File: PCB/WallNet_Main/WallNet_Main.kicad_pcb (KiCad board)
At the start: 4 copper layers, 121.7 x 158.2 mm, 87 parts, among them J1 Conn_01x05_Pin, J101 USB_C_Receptacle_PowerOnly_6P, J102 01x04 Molex, J201 01x04 Molex, J202 Conn_01x07_Socket, J203 02x12 Connector, Q201 BSS138, SW1 SW, U1 BT832, U101 BQ25895RTWT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

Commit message: some random changes
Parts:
- moved R2 120.2 mm to (68.7, 106.0)
- moved D1 118.3 mm to (68.0, 100.5)
- moved C2 38.5 mm to (27.0, 23.5), turned to 90 degrees
- moved R1 33.3 mm to (21.5, 23.0), turned to -90 degrees
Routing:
- net VDD_nrf: track 12.1 -> 9.18 mm, vias 5 -> 4
- net GND: track 7.73 -> 5.27 mm, vias 3 -> 2
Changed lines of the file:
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@@
 	(footprint "Diode_SMD:D_0603_1608Metric"
 		(layer "F.Cu")
-		(at -16.2625 17.5 180)
+		(at 68 100.5 180)
 		(descr "Diode SMD 0603 (1608 Metric), square (rectangular) end terminal, IPC-7351 nominal, (Body size source: http://www.tortai-tech.com/upload/download/2011102023233369053.pdf), generated with kicad-footprint-generator")
 		(tags "diode")
@@
 	(footprint "Resistor_SMD:R_0603_1608Metric"
 		(layer "F.Cu")
-		(at -16.225 21 180)
+		(at 68.7125 106 180)
 		(descr "Resistor SMD 0603 (1608 Metric), square (rectangular) end terminal, IPC-7351 nominal, (Body size source: IPC-SM-782 page 72, https://www.pcb-3d.com/wordpress/wp-content/uploads/ipc-sm-782a_amendment_1_and_2.pdf), generated with kicad-footprint-generator")
 		(tags "resistor")
@@
 	(footprint "Capacitor_SMD:C_0603_1608Metric"
 		(layer "F.Cu")
-		(at -11.4 20.5 180)
+		(at 27 23.5 90)
 		(descr "Capacitor SMD 0603 (1608 Metric), square (rectangular) end terminal, IPC-7351 nominal, (Body size source: IPC-SM-782 page 76, https://www.pcb-3d.com/wordpress/wp-content/uploads/ipc-sm-782a_amendment_1_and_2.pdf), generated with kicad-footprint-generator")
 		(tags "capacitor")
 		(property "Reference" "C2"
-			(at 0 -1.43 0)
+			(at 0 -1.43 90)
 			(layer "F.SilkS")
 			(effects
@@
 		)
 		(property "Value" "100nF"
-			(at -2.85 -0.5 0)
+			(at -2.85 -0.5 90)
 			(layer "F.Fab")
 			(effects
@@
 		)
 		(property "Datasheet" "~"
-			(at 0 0 0)
+			(at 0 0 90)
 			(layer "F.Fab")
 			(hide yes)
@@
 		)
 		(property "Description" "Unpolarized capacitor, small symbol"
-			(at 0 0 0)
+			(at 0 0 90)
 			(layer "F.Fab")
 			(hide yes)
@@
 		(attr smd)
 		(fp_line
-			(start -0.14058 0.51)
-			(end 0.14058 0.51)
+			(start -0.14058 -0.51)
+			(end 0.14058 -0.51)
 			(stroke
 				(width 0.12)
@@
 		)
 		(fp_line
-			(start -0.14058 -0.51)
-			(end 0.14058 -0.51)
+			(start -0.14058 0.51)
+			(end 0.14058 0.51)
 			(stroke
 				(width 0.12)
@@
 		)
 		(fp_text user "${REFERENCE}"
-			(at 0 0 0)
+			(at 0 0 90)
 			(layer "F.Fab")
 			(effects
@@
 		)
 		(pad "1" smd roundrect
-			(at -0.775 0 180)
+			(at -0.775 0 90)
 			(size 0.9 0.95)
 			(layers "F.Cu" "F.Mask" "F.Paste")
@@
 		)
 		(pad "2" smd roundrect
-			(at 0.775 0 180)
+			(at 0.775 0 90)
 			(size 0.9 0.95)
 			(layers "F.Cu" "F.Mask" "F.Paste")
@@
 	(footprint "Resistor_SMD:R_0603_1608Metric"
 		(layer "F.Cu")
-		(at -11.4 17.99 180)
+		(at 21.5 23 -90)
 		(descr "Resistor SMD 0603 (1608 Metric), square (rectangular) end terminal, IPC-7351 nominal, (Body size source: IPC-SM-782 page 72, https://www.pcb-3d.com/wordpress/wp-content/uploads/ipc-sm-782a_amendment_1_and_2.pdf), generated with kicad-footprint-generator")
 		(tags "resistor")
 		(property "Reference" "R1"
-			(at -2.35 -0.01 0)
+			(at -2.35 -0.01 90)
 			(layer "F.SilkS")
 			(effects
@@
 		)
 		(property "Value" "10k"
-			(at 0 1.43 0)
+			(at 0 1.43 90)
 			(layer "F.Fab")
 			(effects
@@
 		)
 		(property "Datasheet" "~"
-			(at 0 0 0)
+			(at 0 0 90)
 			(layer "F.Fab")
 			(hide yes)
@@
 		)
 		(property "Description" "Resistor, small US symbol"
-			(at 0 0 0)
+			(at 0 0 90)
 			(layer "F.Fab")
 			(hide yes)
@@
 		)
 		(fp_text user "${REFERENCE}"
-			(at 0 0 0)
+			(at 0 0 90)
 			(layer "F.Fab")
 			(effects
@@
 		)
 		(pad "1" smd roundrect
-			(at -0.825 0 180)
+			(at -0.825 0 270)
 			(size 0.8 0.95)
 			(layers "F.Cu" "F.Mask" "F.Paste")
@@
 		)
 		(pad "2" smd roundrect
-			(at 0.825 0 180)
+			(at 0.825 0 270)
 			(size 0.8 0.95)
 			(layers "F.Cu" "F.Mask" "F.Paste")
@@
 		(fill no)
 		(layer "F.Cu")
-		(net 1)
+		(net 72)
 	)
 	(gr_rect
@@
 	)
 	(segment
-		(start -15.475 16.075)
-		(end -15.475 17.5)
-		(width 0.1524)
-		(layer "F.Cu")
-		(net 1)
-	)
-	(segment
 		(start 15 47)
 		(end 18 47)
@@
 	)
 	(segment
-		(start -13.05 20.5)
-		(end -12.175 20.5)
-		(width 0.1524)
-		(layer "F.Cu")
-		(net 1)
-	)
-	(segment
 		(start 68 85.675)
 		(end 68 84.825)
@@
 		(net 1)
 	)
-	(segment
-		(start 37.345 27.01)
-		(end 37.5 27.01)
-		(width 0.1524)
-		(layer "F.Cu")
-		(net 1)
-	)
 	(via
 		(at 68 85.675)
@@
 		(net 1)
 	)
-	(via
-		(at -13.05 20.5)
-		(size 0.6)
-		(drill 0.3)
-		(layers "F.Cu" "B.Cu")
-		(net 1)
-	)
 	(segment
 		(start 20.5 27.9)
@@
 	)
 	(segment
-		(start -10.575 17.99)
-		(end -10.575 20.45)
-		(width 0.1524)
-		(layer "F.Cu")
-		(net 65)
-	)
-	(segment
 		(start 22.04 51.5)
 		(end 22.04 53.5)
@@
 	)
 	(segment
-		(start -10.575 20.45)
-		(end -10.625 20.5)
-		(width 0.1524)
-		(layer "F.Cu")
-		(net 65)
-	)
-	(segment
 		(start 50.5 19)
 		(end 51.675 19)
@@
 	)
 	(segment
-		(start 27.3 23.25)
-		(end 27.5796 23.5296)
-		(width 0.1524)
-		(layer "F.Cu")
-		(net 65)
-	)
-	(segment
 		(start 19.5 66)
 		(end 20.825 66)
@@
 		(size 0.6)
 		(drill 0.3)
-		(layers "F.Cu" "B.Cu")
-		(net 65)
-	)
-	(via
-		(at -10.55 19)
-		(size 0.6)
-		(drill 0.3)

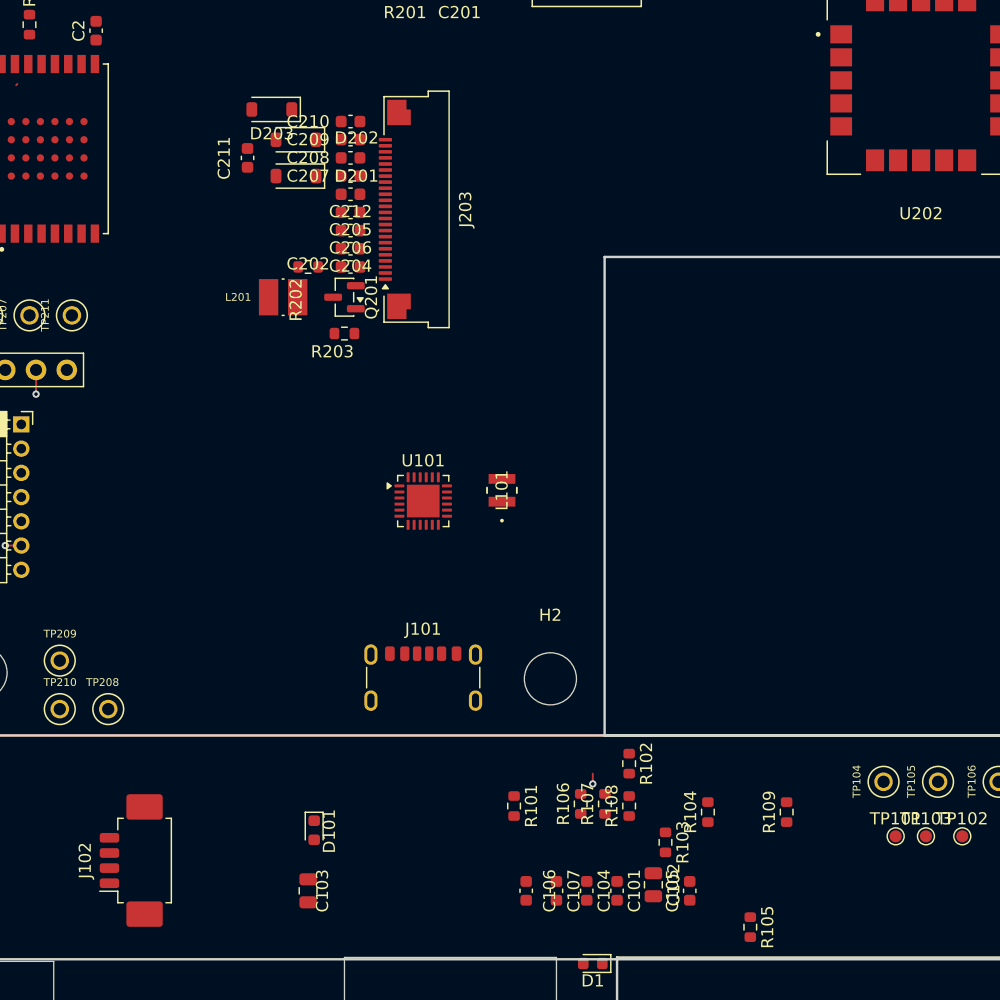
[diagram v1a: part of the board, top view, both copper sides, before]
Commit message: Added discreet components around BMU
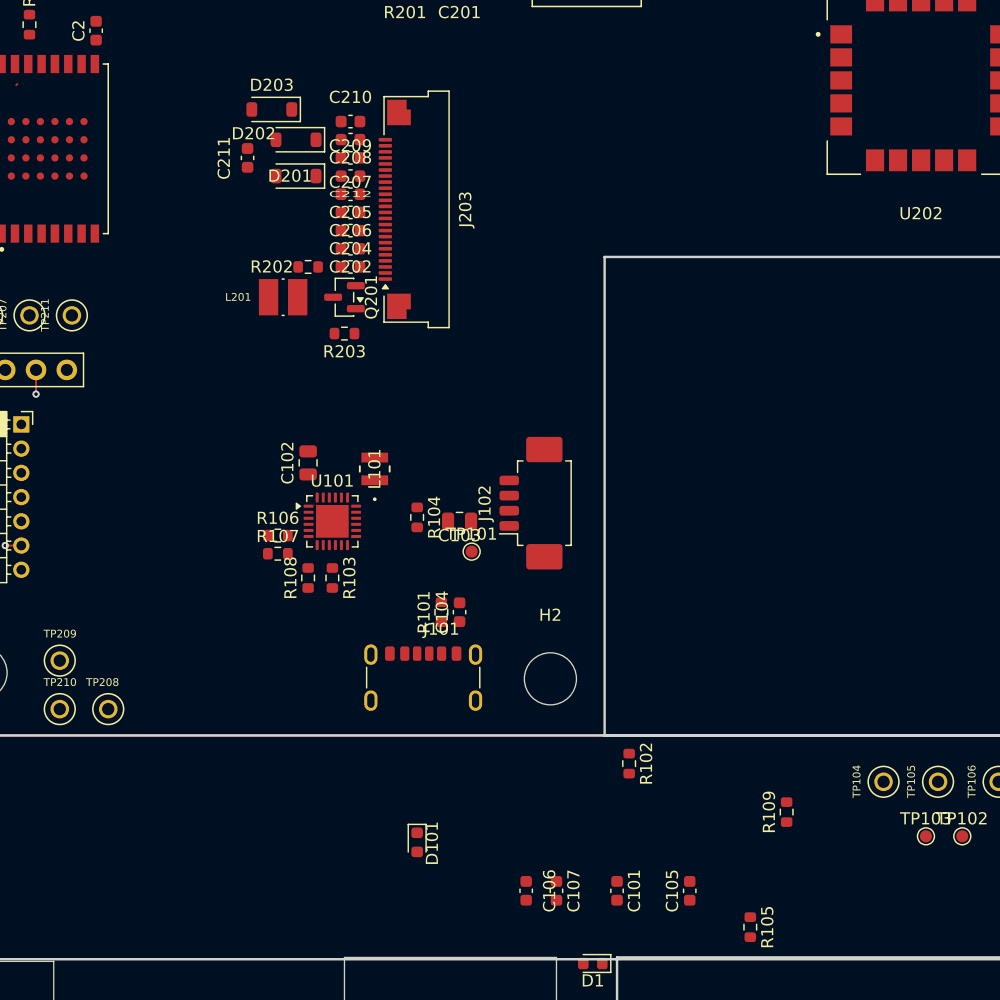
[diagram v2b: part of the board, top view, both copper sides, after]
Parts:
- moved C102 45.0 mm to (44.5, 59.2), turned to 90 degrees
- moved J102 44.3 mm to (63.5, 62.5)
- moved TP101 42.2 mm to (58.0, 66.5)
- moved R103 35.1 mm to (46.5, 68.7)
- moved R104 34.2 mm to (53.5, 63.7), turned to -90 degrees
- moved R107 34.0 mm to (42.0, 66.7), turned to 0 degrees
- moved R106 33.4 mm to (42.0, 65.2), turned to 0 degrees
- moved C103 33.0 mm to (57.0, 64.0), turned to 180 degrees
- moved R108 32.5 mm to (44.5, 68.7)
- moved C104 25.3 mm to (57.0, 71.5), turned to 90 degrees
- moved R101 17.1 mm to (55.5, 71.5), turned to 90 degrees
- moved L101 10.6 mm to (50.0, 59.7)
- moved D101 8.56 mm to (53.5, 90.5)
- moved U101 7.68 mm to (46.5, 64.0)
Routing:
- net GND: track 5.27 -> 4.42 mm, vias 2 -> 1

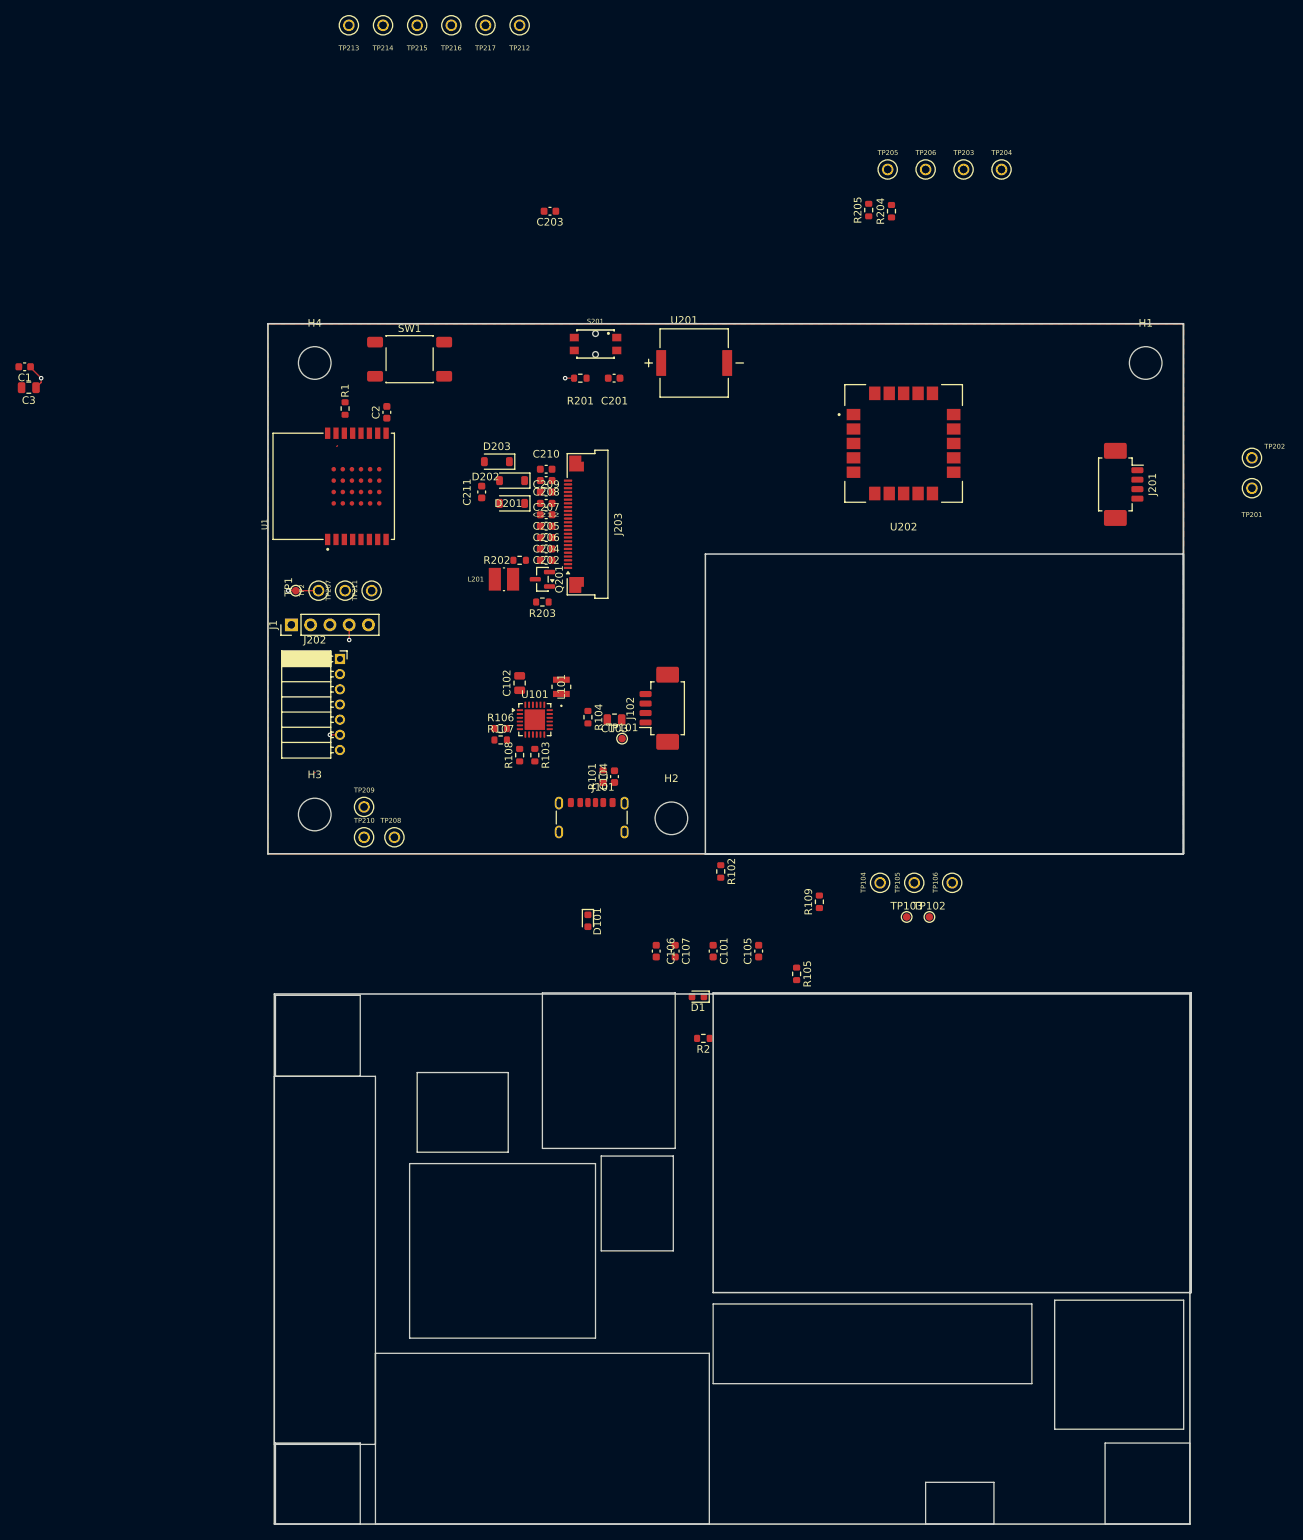
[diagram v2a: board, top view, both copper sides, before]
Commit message: finished layout of pcb
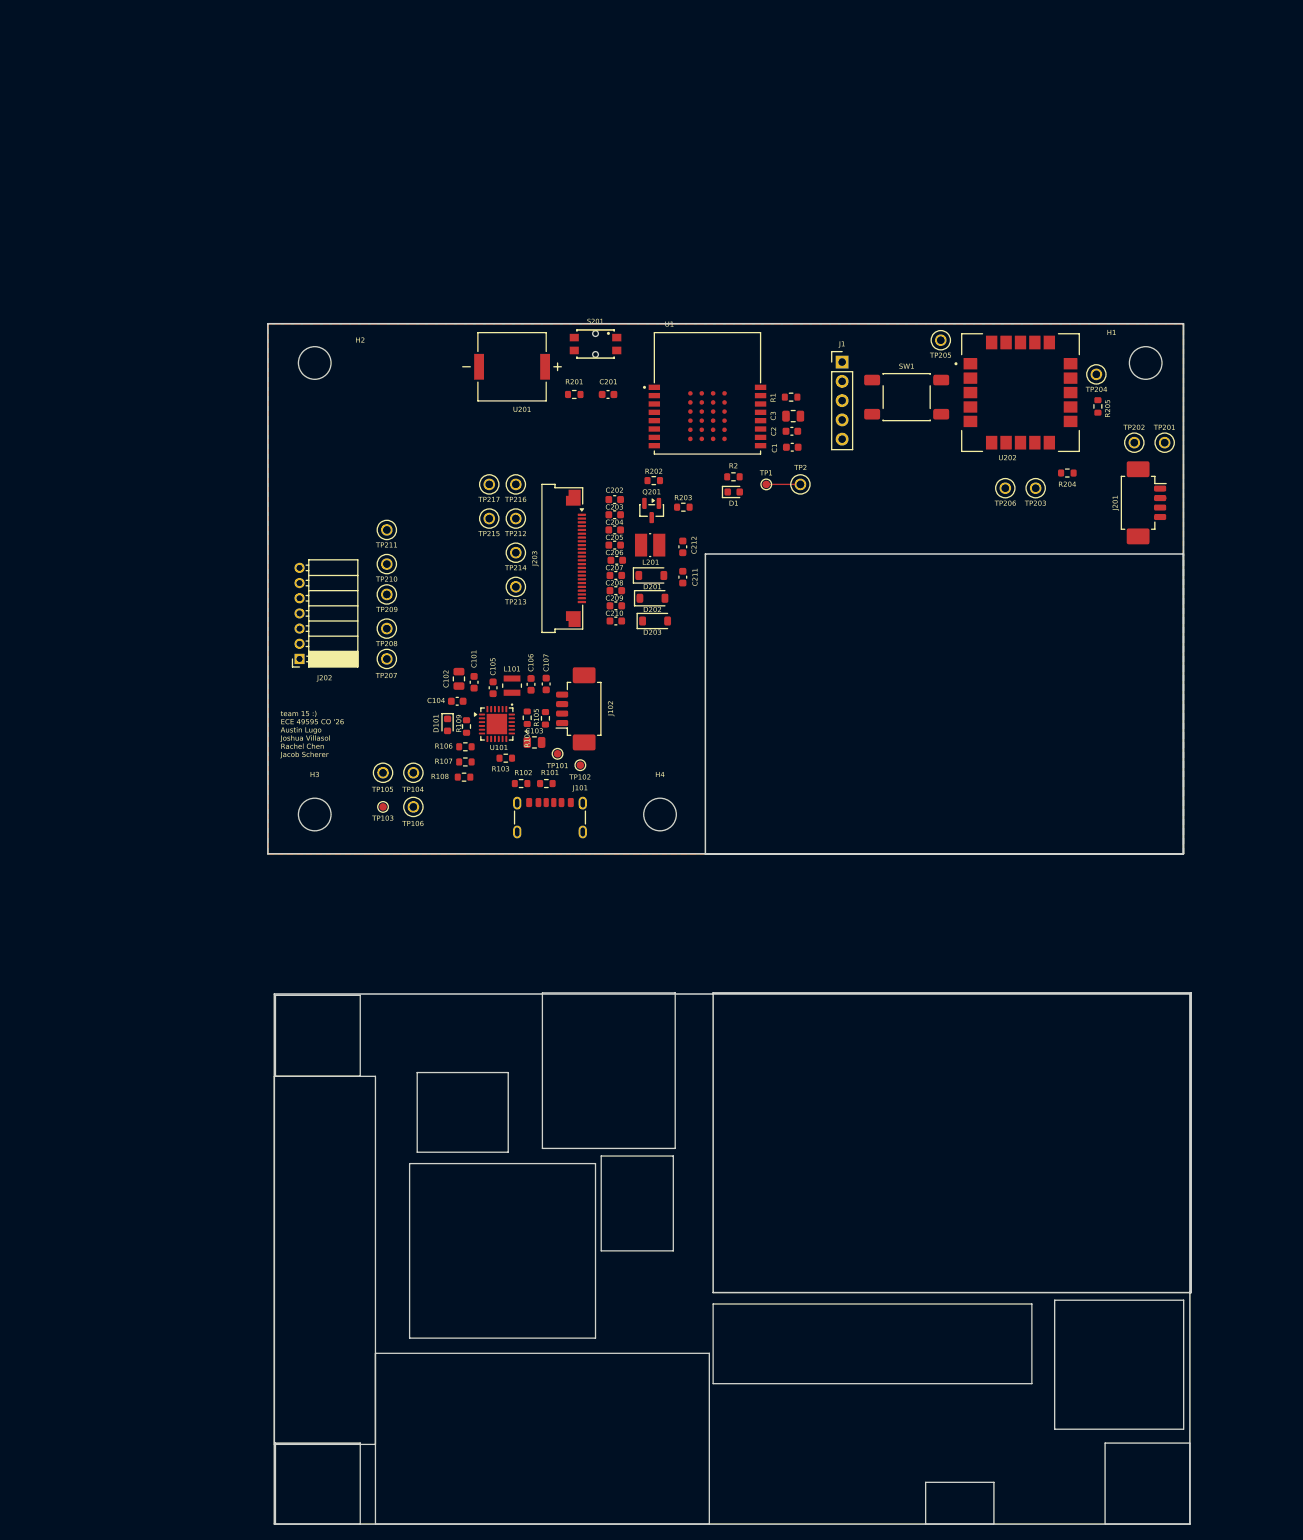
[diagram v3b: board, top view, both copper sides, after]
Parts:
- removed the H2 at (64.5, 77.0)
- added H4: MountingHole, MountingHole:MountingHole_4.3mm_M4, F.Cu at (63.0, 76.5)
- J101: value USB_C_Receptacle_PowerOnly_6P -> usbc_plug_lfg
- moved C1 101.7 mm to (80.4, 28.1), turned to 0 degrees
- moved C3 100.8 mm to (80.5, 24.0), turned to 0 degrees
- moved J1 80.4 mm to (87.0, 16.9), turned to 0 degrees
- moved TP213 77.2 mm to (44.0, 46.5)
- moved R2 74.1 mm to (72.7, 32.0), turned to 0 degrees
- moved TP106 71.7 mm to (30.5, 75.5), turned to 180 degrees
- moved TP214 71.7 mm to (44.0, 42.0)
- moved TP105 71.5 mm to (26.5, 71.0), turned to 180 degrees
- moved TP103 70.5 mm to (26.5, 75.5)
- moved D1 66.7 mm to (72.7, 34.0), turned to 0 degrees
- moved SW1 65.7 mm to (95.5, 21.5)
- moved TP215 65.7 mm to (40.5, 37.5)
- moved TP2 65.0 mm to (81.5, 33.0), turned to 0 degrees
- moved TP212 65.0 mm to (44.0, 37.5)
- moved TP1 63.6 mm to (77.0, 33.0), turned to 0 degrees
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- renumbered H4 to H2
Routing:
- net VDD_nrf: track 9.18 -> 0.10 mm, vias 4 -> 0
- net /P12: track 0.00 -> 0.80 mm
- net GND: track 4.42 -> 4.50 mm, vias 1 -> 0
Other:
- board text added: "team 15 :) ECE 49595 CO '26 Austin Lugo Joshua Villasol Rachel Chen Jacob Scherer"

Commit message: Accident
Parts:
- removed the H4 at (63.0, 76.5)
- added H2: MountingHole, MountingHole:MountingHole_4.3mm_M4, F.Cu at (64.5, 77.0)
- J101: value usbc_plug_lfg -> USB_C_Receptacle_PowerOnly_6P
- moved C1 101.7 mm to (-20.7, 17.5), turned to 180 degrees
- moved C3 100.8 mm to (-20.2, 20.2), turned to 180 degrees
- moved J1 80.4 mm to (14.4, 51.5), turned to 90 degrees
- moved TP213 77.2 mm to (22.0, -27.5)
- moved R2 74.1 mm to (68.7, 106.0), turned to 180 degrees
- moved TP106 71.7 mm to (101.5, 85.5), turned to 90 degrees
- moved TP214 71.7 mm to (26.5, -27.5)
- moved TP105 71.5 mm to (96.5, 85.5), turned to 90 degrees
- moved TP103 70.5 mm to (95.5, 90.0)
- moved D1 66.7 mm to (68.0, 100.5), turned to 180 degrees
- moved SW1 65.7 mm to (30.0, 16.5)
- moved TP215 65.7 mm to (31.0, -27.5)
- moved TP2 65.0 mm to (18.0, 47.0), turned to 90 degrees
- moved TP212 65.0 mm to (44.5, -27.5)
- moved TP1 63.6 mm to (15.0, 47.0), turned to 90 degrees
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- renumbered H2 to H4
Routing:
- net VDD_nrf: track 0.10 -> 9.18 mm, vias 0 -> 4
- net /P12: track 0.80 -> 0.00 mm
- net GND: track 4.50 -> 4.42 mm, vias 0 -> 1
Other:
- board text removed: "team 15 :) ECE 49595 CO '26 Austin Lugo Joshua Villasol Rachel Chen Jacob Scherer"
